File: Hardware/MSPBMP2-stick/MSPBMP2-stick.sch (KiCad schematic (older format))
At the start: 54 parts, among them J1 48037-0001, J2 JTAG, J3 SWD, U1 STM32L432KBU6, U2 LD1117AG-33-AB3-A-R, U3 AD8531ARTZ, U4 TXS0108EPWR, Y1 32768

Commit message: Schema update of PCB-Stick
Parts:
- removed R11: 47K, Resistor_SMD:R_0402_1005Metric_Pad0.72x0.64mm_HandSolder, symbol Device:R
- C1: value 220nF -> 100nF; Descr Multilayer Ceramic Capacitors MLCC - SMD/SMT 220nF 16V 0402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 -> 100nF ±10% 16V X7R 0402 Multilayer Ceramic Capacitors MLCC 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; LCSC C16772 -> C1525
- C12: renamed from C10; value 1.2pF -> 4.7pF; Descr 1.5pF ±0.25pF 50V C0G 0402 Multilayer Ceramic Capacitors ML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 -> 4.7pF ±0.25pF 50V C0G 0402 Multilayer Ceramic Capacitors ML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; LCSC C1552 -> C1569
- C13: renamed from C11; value 1.2pF -> 4.7pF; Descr 1.5pF ±0.25pF 50V C0G 0402 Multilayer Ceramic Capacitors ML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 -> 4.7pF ±0.25pF 50V C0G 0402 Multilayer Ceramic Capacitors ML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; LCSC C1552 -> C1569
- RN1, RN2: footprint Resistor_SMD:R_Array_Convex_4x0402 -> LocalLib:R_Array_Convex_4x0402_hand_soldered
- U1: renamed from U2; value LD1117AG-33-AB3-A-R -> AMS1117-3.3; Descr Fixed 15V 3.3V 1.3V @ 1A SOT-89(SOT-89-3) Dropout Regulator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 -> Fixed 10V 3.3V 1.3V @ 1A SOT-89 Dropout Regulators(LDO) RoHS; LCSC C81768 -> C347256
- U2: renamed from U1; Descr (none) -> 32-Bit FLASH ARM® Cortex®-M4 80MHz 1.71V ~ 3.6V UFQFPN-32 S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; LCSC (none) -> C94784
- U3: footprint Package_TO_SOT_SMD:TSOT-23-5_HandSoldering -> Package_TO_SOT_SMD:SOT-23-5_HandSoldering
- Y1: value 32768 -> 32768 7pF; Descr 32.768KHz ±20ppm 12.5pF 70kΩ 3215 SMD Crystal Resonators Ro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 -> 32.768KHz ±20ppm 7pF 70kΩ SMD-3215_2P SMD Crystal Resonator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; LCSC C271654 -> C97604
- renumbered C13 to C10, C8 to C11, C3 to C2, C4 to C3, C6 to C4, C9 to C5, C2 to C6, C12 to C7, C5 to C8, C7 to C9, R2 to R1, R10 to R11, R3 to R2, R1 to R3, R7 to R4, R4 to R5, R5 to R7, R9 to R8, R8 to R9
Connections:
- net +3V3: now also C15.2, C16.2, U4.19 (VCCB); no longer C15.1, C16.1, U4.2 (VCCA)
- net GND: now also C15.1, C16.1; no longer C15.2, C16.2
- net JRST: now also U4.17 (B3); no longer U4.7 (A6)
- net JRXD: now also U4.20 (B1); no longer U4.8 (A7)
- net JTCK: now also U4.15 (B5); no longer U4.5 (A4)
- net JTDI: now also U4.13 (B7); no longer U4.3 (A2)
- net JTDO: now also U4.12 (B8); no longer U4.1 (A1)
- net JTEST: now also U4.16 (B4); no longer U4.6 (A5)
- net JTMS: now also U4.14 (B6); no longer U4.4 (A3)
- net JTXD: now also U4.18 (B2); no longer U4.9 (A8)
- net VCC_TOOL: now also U4.10 (OE), U4.2 (VCCA); no longer U4.19 (VCCB)
- net LRXD: now reaches RN2.4 (R4.1)
- net LRXD: now also U4.1 (A1); no longer U4.12 (B8)
- net LTXD: now reaches RN2.3 (R3.1)
- net LTXD: now also U4.3 (A2); no longer U4.13 (B7)
- net LRST: now reaches RN2.2 (R2.1)
- net LRST: now also U4.4 (A3); no longer U4.14 (B6)
- net LTEST: now reaches RN2.1 (R1.1)
- net LTEST: now also U4.5 (A4); no longer U4.15 (B5)
- net LTCK: now reaches RN1.4 (R4.1)
- net LTCK: now also U4.6 (A5); no longer U4.16 (B4)
- net LTMS: now reaches RN1.3 (R3.1)
- net LTMS: now also U4.7 (A6); no longer U4.17 (B3)
- net LTDI: now reaches RN1.2 (R2.1)
- net LTDI: now also U4.8 (A7); no longer U4.18 (B2)
- net LTDO: now reaches RN1.1 (R1.1)
- net LTDO: now also U4.9 (A8); no longer U4.20 (B1)
- net JENA: no longer names the net of U2.15 (PB1)
- net JENA: no longer U4.10 (OE)
- no-connect marks 7 -> 8
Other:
- moved on the sheet: C1, C10, C11, C12, C13, C14, C15, C16, C18, C2, C20, C21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

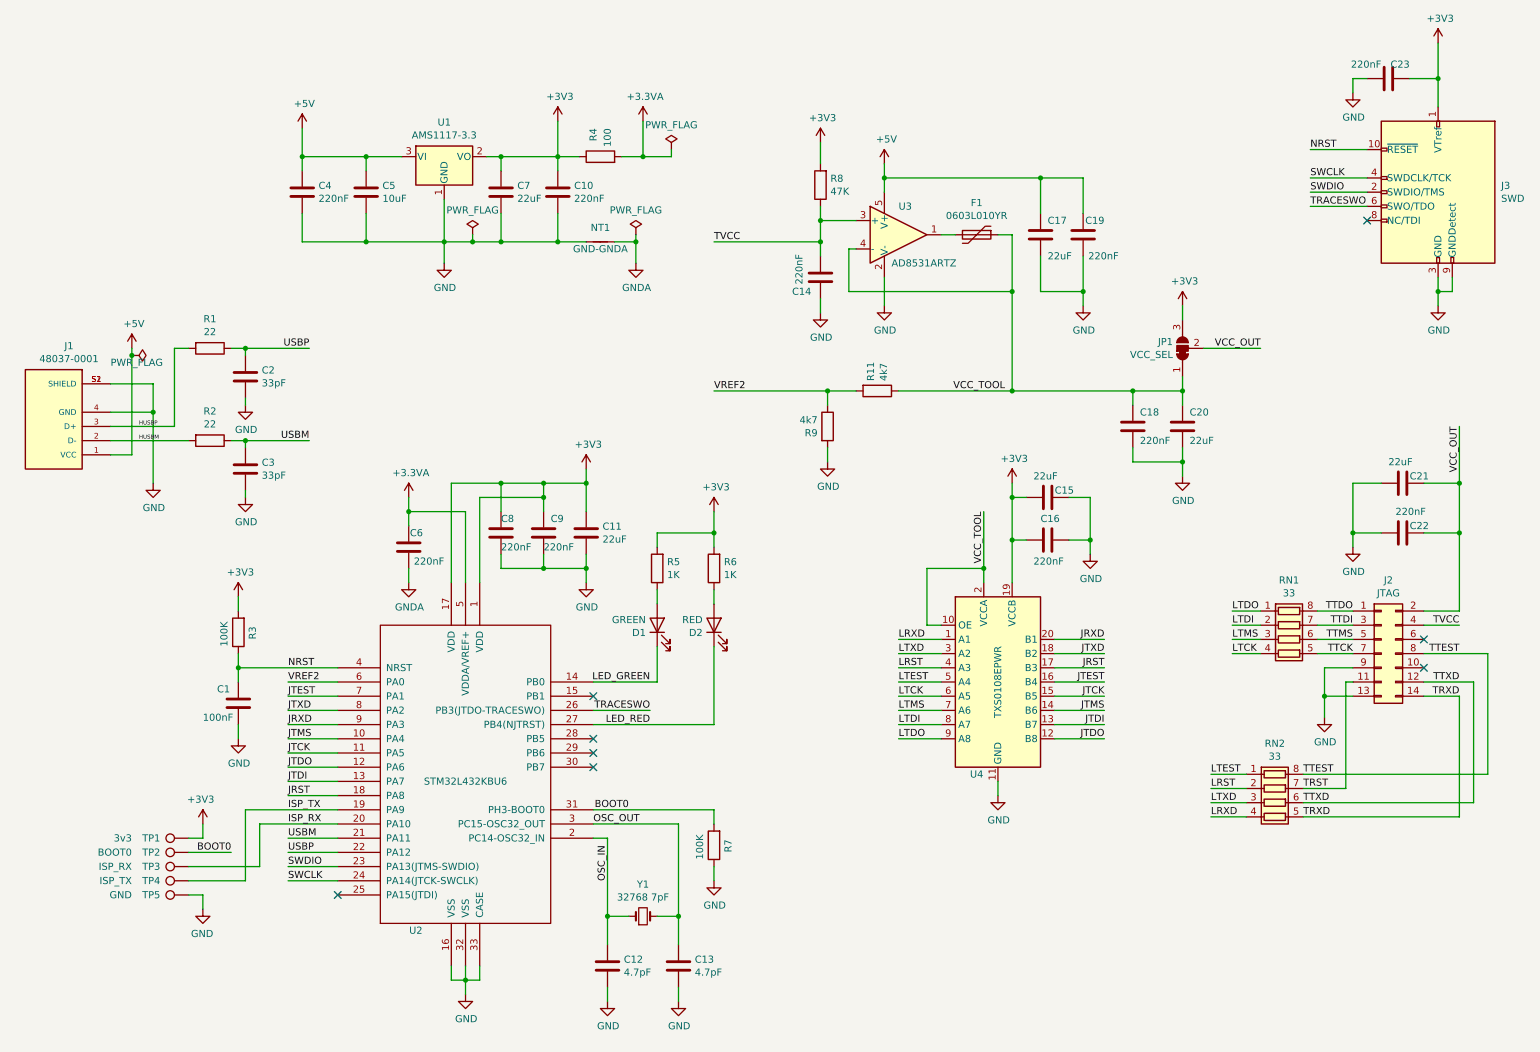
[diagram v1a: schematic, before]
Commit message: Hardware V2 improvements (component values and sizes, layout and review of V-Target circuitry).
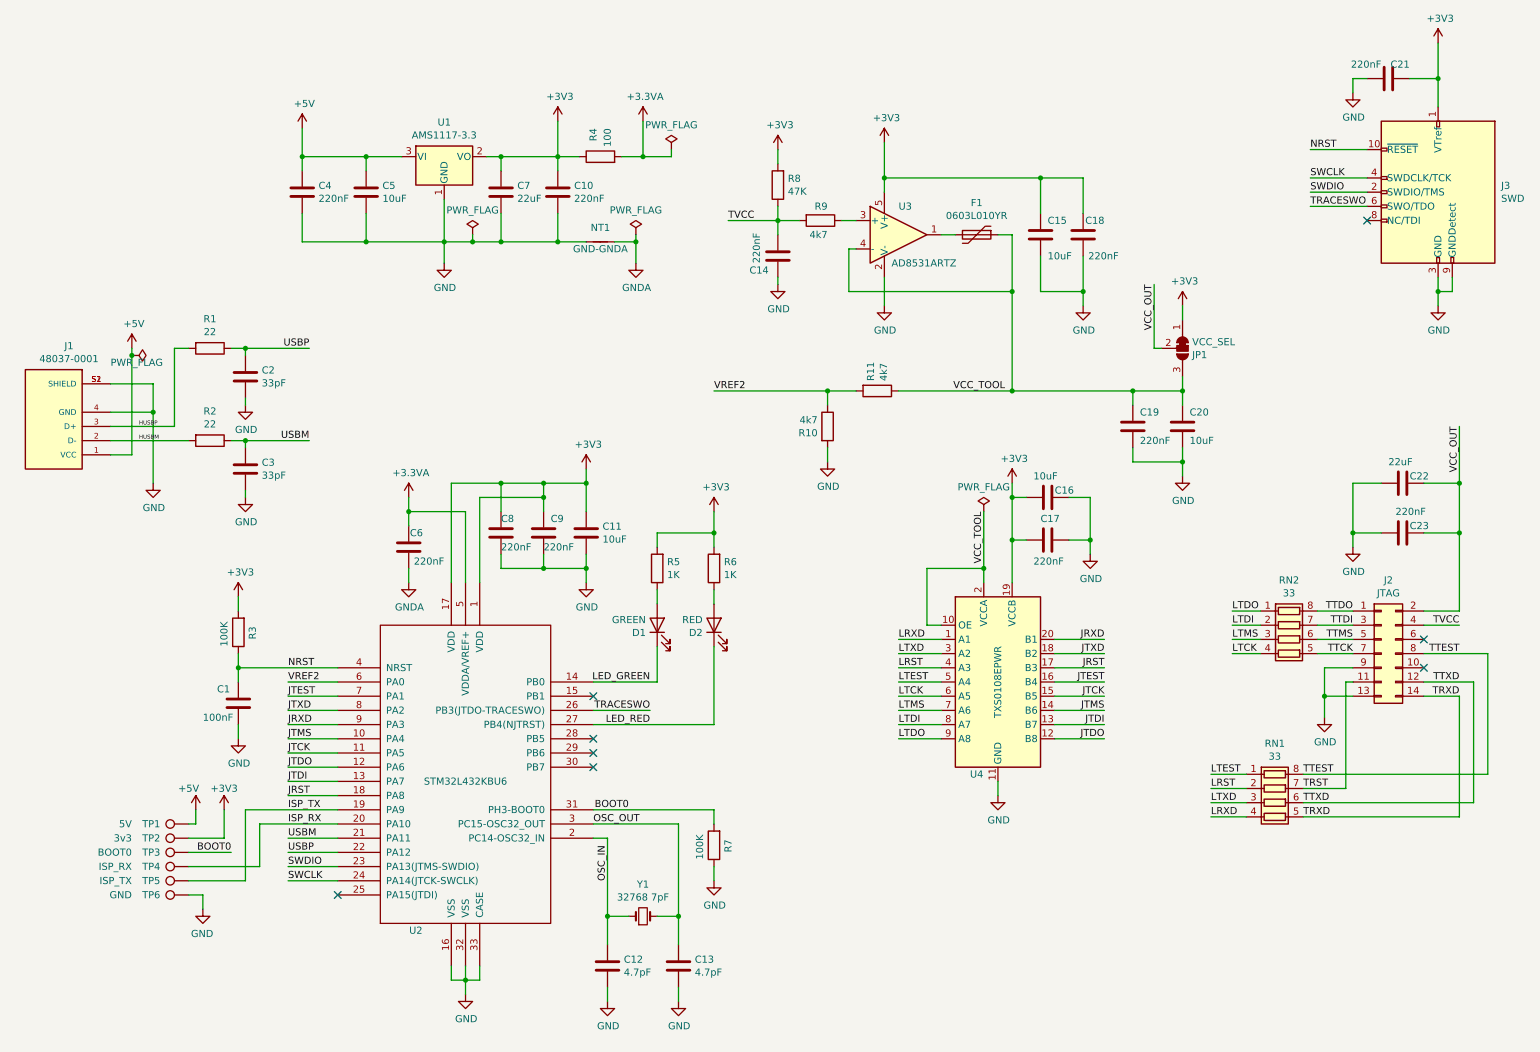
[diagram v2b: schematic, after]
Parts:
- added R9: 4k7, Resistor_SMD:R_0402_1005Metric_Pad0.72x0.64mm_HandSolder, symbol Device:R
- added TP1: 5V, TestPoint:TestPoint_Pad_D1.5mm, symbol Connector:TestPoint
- C11, C20: value 22uF -> 10uF; footprint Capacitor_SMD:C_0603_1608Metric_Pad1.08x0.95mm_HandSolder -> Capacitor_SMD:C_0402_1005Metric_Pad0.74x0.62mm_HandSolder; Descr 22uF ±20% 6.3V X5R 0603 Multilayer Ceramic Capacitors MLCC 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 -> 10uF ±20% 6.3V X5R 0402 Multilayer Ceramic Capacitors MLCC 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; LCSC C59461 -> C15525
- C15: renamed from C17; value 22uF -> 10uF; footprint Capacitor_SMD:C_0603_1608Metric_Pad1.08x0.95mm_HandSolder -> Capacitor_SMD:C_0402_1005Metric_Pad0.74x0.62mm_HandSolder; Descr 22uF ±20% 6.3V X5R 0603 Multilayer Ceramic Capacitors MLCC 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 -> 10uF ±20% 6.3V X5R 0402 Multilayer Ceramic Capacitors MLCC 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; LCSC C59461 -> C15525
- C16: renamed from C15; value 22uF -> 10uF; footprint Capacitor_SMD:C_0603_1608Metric_Pad1.08x0.95mm_HandSolder -> Capacitor_SMD:C_0402_1005Metric_Pad0.74x0.62mm_HandSolder; Descr 22uF ±20% 6.3V X5R 0603 Multilayer Ceramic Capacitors MLCC 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 -> 10uF ±20% 6.3V X5R 0402 Multilayer Ceramic Capacitors MLCC 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; LCSC C59461 -> C15525
- renumbered C16 to C17, C19 to C18, C18 to C19, C23 to C21, C21 to C22, C22 to C23, R9 to R10, RN2 to RN1, RN1 to RN2, TP1 to TP2, TP2 to TP3, TP3 to TP4, TP4 to TP5, TP5 to TP6
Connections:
- net +3V3: now also C15.1, C18.2, JP1.1 (A), U3.5 (V+); no longer JP1.3 (B)
- net +5V: now also TP1.1; no longer C15.1, C18.2, U3.5 (V+)
- net TVCC: now also R9.2; no longer U3.3 (+)
- net VCC_TOOL: now also JP1.3 (B); no longer JP1.1 (A)
- new net: R9.1, U3.3 (+)
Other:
- moved on the sheet: C14, JP1, R8
